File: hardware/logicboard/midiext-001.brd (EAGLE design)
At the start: 72 x 72 mm, 29 parts, among them IC1 74ALS05N, IC2 LTC485N, IC3 LTC485N, J1 PWR, J2 MIDIOUT, J3 MIDIIN, J4 LED, J5 MIDIRX, J6 MIDITX, J7 LED

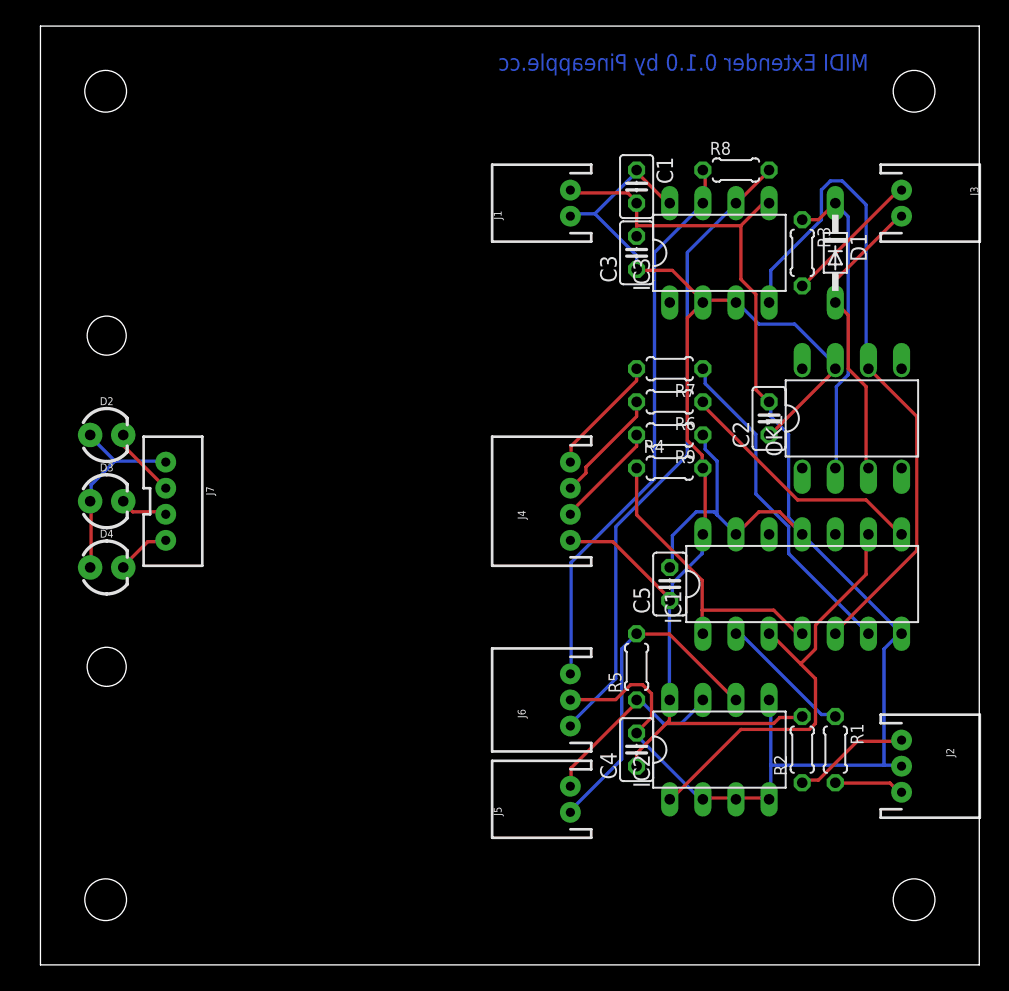
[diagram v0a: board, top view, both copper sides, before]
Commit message: Removed LED panel from main logic board.
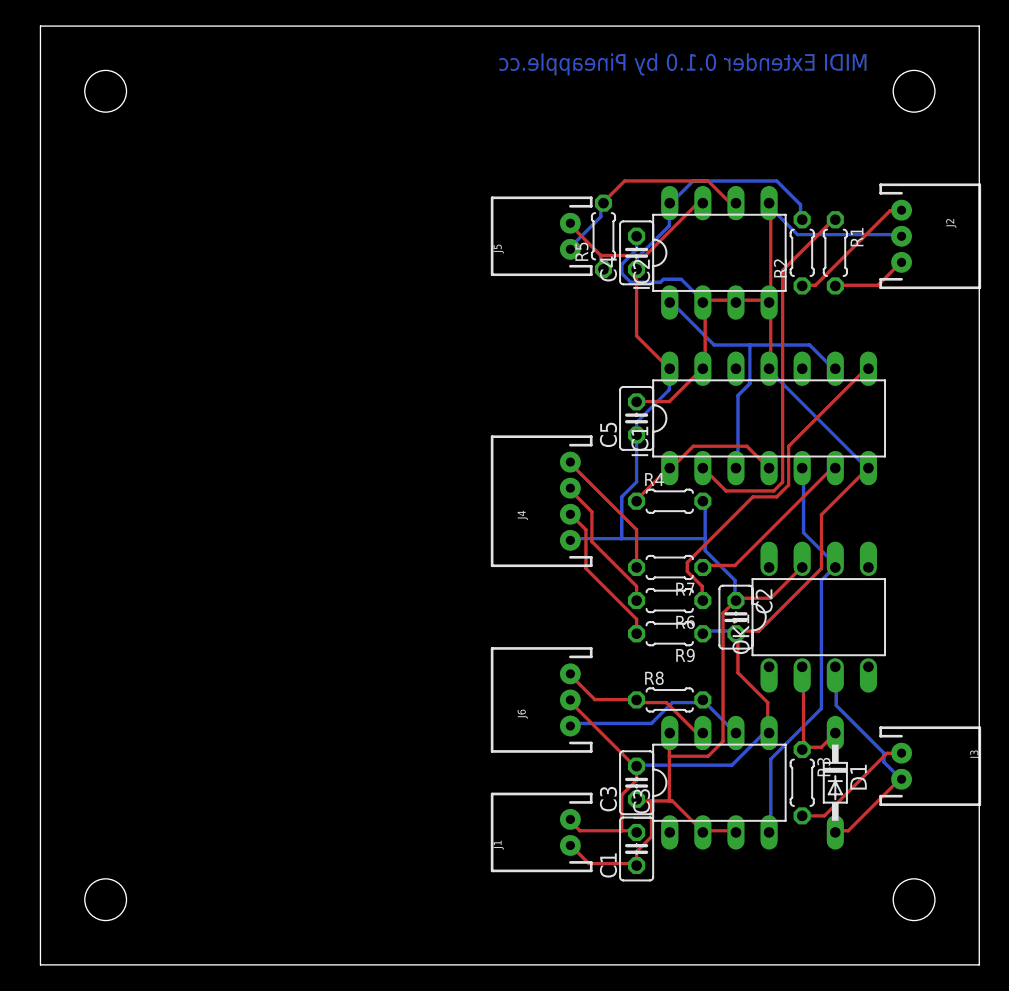
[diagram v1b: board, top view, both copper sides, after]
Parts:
- removed D2: PWR, SparkFun-LED:LED_3MM
- removed D3: OUT, SparkFun-LED:LED_3MM
- removed D4: IN, SparkFun-LED:LED_3MM
- removed J7: LED, SparkFun-Connectors:JST-4-PTH-VERT
- moved C1 50.8 mm to (45.7, 8.89), turned to 90 degrees
- moved J1 48.3 mm to (40.6, 10.2)
- moved J5 43.2 mm to (40.6, 55.9)
- moved J3 43.2 mm to (66.0, 15.2)
- moved R8 41.0 mm to (48.3, 20.3)
- moved C3 40.6 mm to (45.7, 14.0)
- moved D1 40.6 mm to (61.0, 14.0)
- moved IC3 40.6 mm to (52.1, 14.0)
- moved J2 40.6 mm to (66.0, 55.9)
- moved R3 40.6 mm to (58.4, 14.0)
- moved C4 38.1 mm to (45.7, 54.6)
- moved IC2 38.1 mm to (52.1, 54.6)
- moved R1 38.1 mm to (61.0, 54.6)
- moved R2 38.1 mm to (58.4, 54.6)
- moved R5 33.1 mm to (43.2, 55.9)
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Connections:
- removed net N$11: D3.K, J7.3
- removed net N$12: D4.K, J7.4
- removed net N$4: D2.A, D3.A, D4.A, J7.1
- removed net N$5: D2.K, J7.2
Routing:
- net TX+: track 48.9 -> 14.7 mm
- net TX-: track 43.0 -> 12.2 mm
- net COM2: track 52.0 -> 31.2 mm
- net N$2: track 10.4 -> 29.0 mm
- net N$4: track 15.7 -> 0.00 mm
- net N$15: track 24.2 -> 9.38 mm
- net N$6: track 25.7 -> 13.4 mm
- net N$3: track 23.2 -> 12.7 mm
- net N$1: track 34.1 -> 24.7 mm
- net RX+: track 25.5 -> 16.2 mm
- net GND: track 129.2 -> 122.1 mm
- net VCC: track 101.5 -> 108.3 mm
- net N$7: track 19.6 -> 25.2 mm
- net N$5: track 5.42 -> 0.00 mm
- net MIDIRX-: track 22.6 -> 17.6 mm
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
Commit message: Fixed values.
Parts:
- R6, R7, R9: value 220 -> 330
- moved C1 35.7 mm to (10.2, 11.4)
- moved C2 35.7 mm to (17.8, 29.2)
- moved C3 35.7 mm to (10.2, 16.5)
- moved C4 35.7 mm to (10.2, 57.1)
- moved C5 35.7 mm to (10.2, 44.5)
- moved D1 35.7 mm to (25.4, 16.5)
- moved IC1 35.7 mm to (20.3, 44.5)
- moved IC2 35.7 mm to (16.5, 57.1)
- moved IC3 35.7 mm to (16.5, 16.5)
- moved J1 35.7 mm to (5.08, 12.7)
- moved J2 35.7 mm to (30.5, 58.4)
- moved J3 35.7 mm to (30.5, 12.7)
- moved J4 35.7 mm to (5.08, 38.1)
- moved J5 35.7 mm to (5.08, 58.4)
- moved J6 35.7 mm to (5.08, 22.9)
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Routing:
- net MIDIRX-: track 17.6 -> 19.3 mm
- net MIDIRX+: track 9.61 -> 8.20 mm
- net GND: track 122.1 -> 121.4 mm
- net N$7: track 25.2 -> 24.5 mm
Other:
- board size 72 x 72 mm -> 36 x 72 mm
- board text added: "LED"
- board text added: "MIDI Extender 1.0.0 by Pineapple"
- board text added: "MIDIIN"
- board text added: "MIDIOUT"
- board text added: "PWR"
- board text added: "RX"
- board text added: "TX"
- board text removed: "MIDI Extender 0.1.0 by Pineapple.cc"

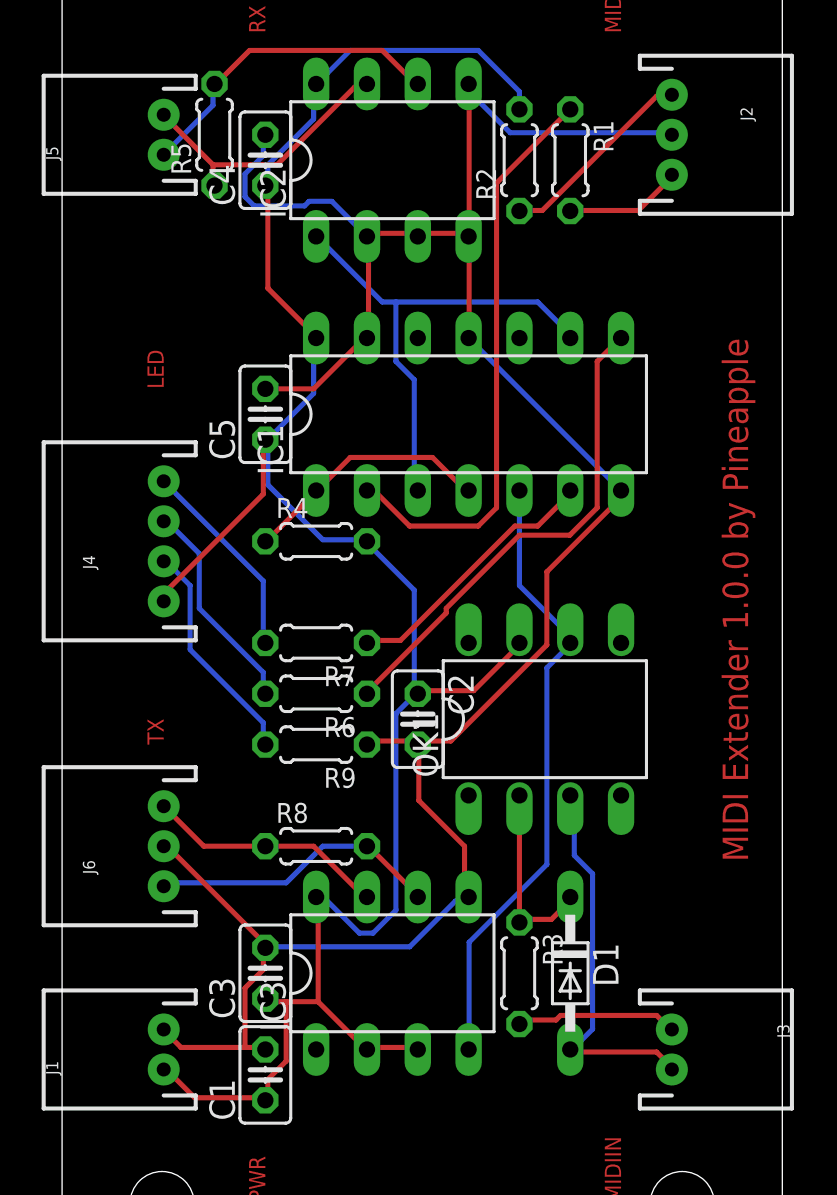
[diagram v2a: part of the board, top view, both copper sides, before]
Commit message: Renumbered components.
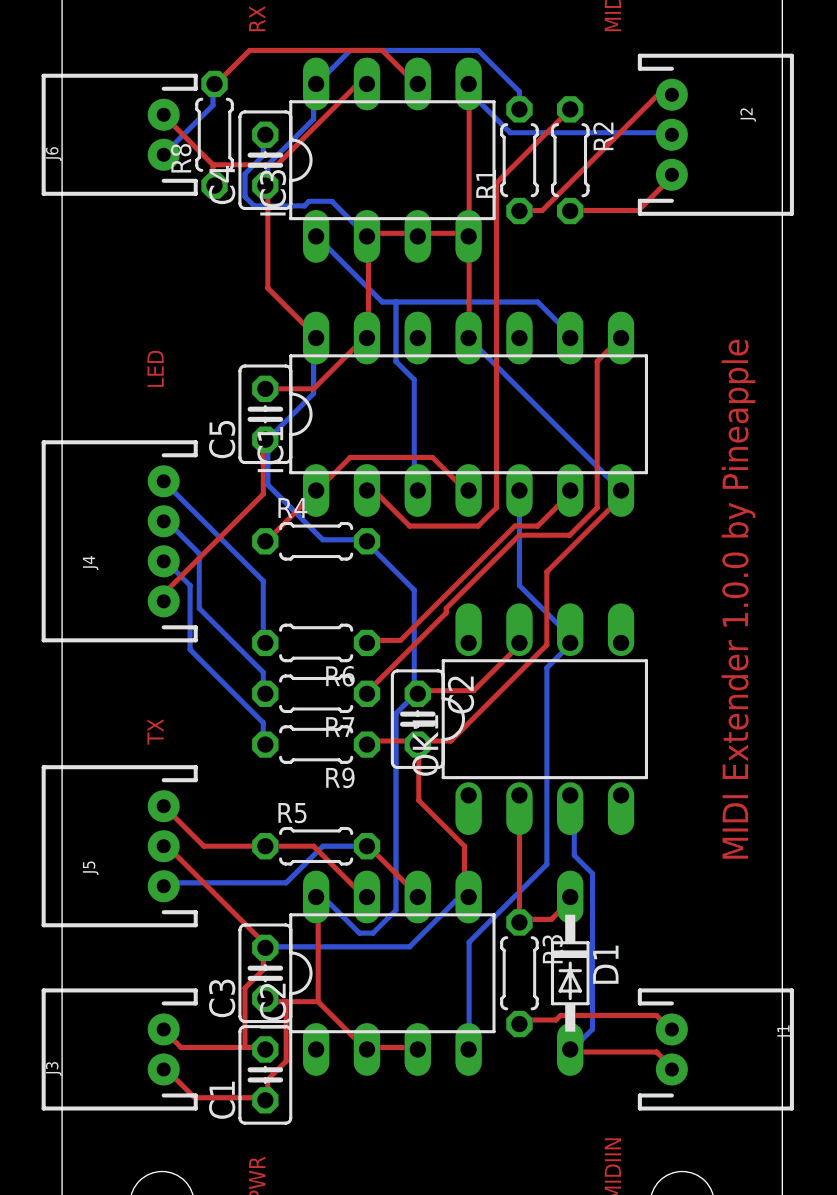
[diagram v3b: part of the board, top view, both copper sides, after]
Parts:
- J1: value PWR -> MIDIIN
- J3: value MIDIIN -> PWR
- J5: value MIDIRX -> MIDITX; device SparkFun-Connectors:JST-2-PTH -> SparkFun-Connectors:JST-3-PTH
- J6: value MIDITX -> MIDIRX; device SparkFun-Connectors:JST-3-PTH -> SparkFun-Connectors:JST-2-PTH
- R4: value 220 -> 10k
- moved IC2 40.6 mm to (16.5, 16.5)
- moved IC3 40.6 mm to (16.5, 57.1)
- moved R5 35.9 mm to (12.7, 22.9), turned to 0 degrees
- moved R8 35.9 mm to (7.62, 58.4), turned to 90 degrees
- moved J5 35.6 mm to (5.08, 22.9)
- moved J6 35.6 mm to (5.08, 58.4)
- moved J1 25.4 mm to (30.5, 12.7), turned to 270 degrees
- moved J3 25.4 mm to (5.08, 12.7), turned to 90 degrees
- moved R6 2.54 mm to (12.7, 33.0)
- moved R7 2.54 mm to (12.7, 30.5)
- moved R1 2.54 mm to (22.9, 57.1), turned to 90 degrees
- moved R2 2.54 mm to (25.4, 57.1), turned to 270 degrees
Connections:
- net COM2: now also IC2.4; no longer IC3.4
- net GND: now also IC3.2, IC3.3, IC3.4, J3.2, J5.2; no longer IC2.2, IC2.3, IC2.4, J1.2, J6.2
- net MIDIRX+: now also J1.1; no longer J3.1
- net MIDIRX-: now also J1.2; no longer J3.2
- net MIDITX+: now also R1.1; no longer R2.1
- net MIDITX-: now also R2.2; no longer R1.2
- net N$1: now also IC3.1; no longer IC2.1
- net N$2: now also R2.1; no longer R1.1
- net N$6: now also R6.1; no longer R7.1
- net N$7: now also R7.1; no longer R6.1
- net N$8: now also R6.2; no longer R7.2
- net N$9: now also R7.2; no longer R6.2
- net RX+: now also IC3.6, J6.1, R8.2; no longer IC2.6, J5.1, R5.2
- net RX-: now also IC3.7, J6.2, R8.1; no longer IC2.7, J5.2, R5.1
- net TX+: now also IC2.6, J5.1, R5.2; no longer IC3.6, J6.1, R8.2
- net TX-: now also IC2.7, J5.3, R5.1; no longer IC3.7, J6.3, R8.1
- net VCC: now also IC2.2, IC2.3, J3.1, R1.2; no longer IC3.2, IC3.3, J1.1, R2.2

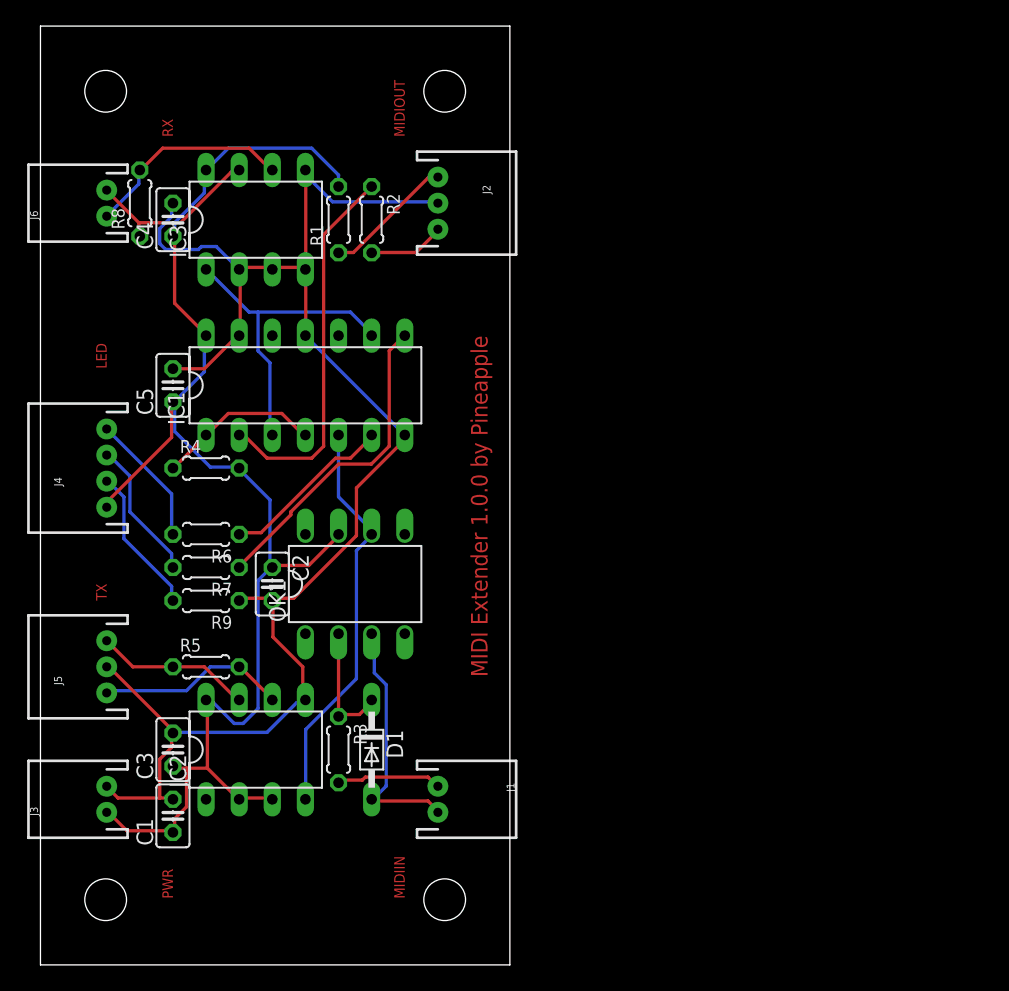
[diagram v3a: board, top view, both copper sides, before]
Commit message: Changed layout.
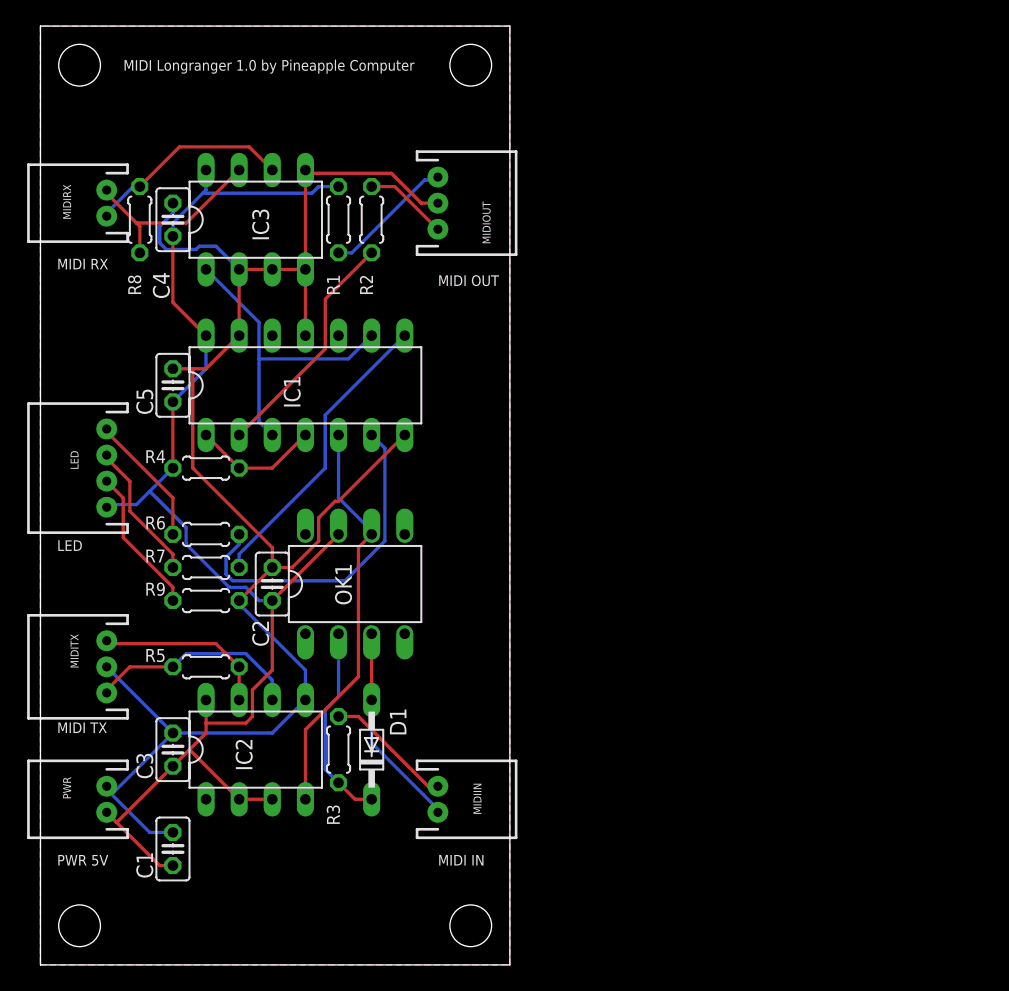
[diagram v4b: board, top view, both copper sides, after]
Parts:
- LED: value LED -> (none)
- MIDIIN: value MIDIIN -> (none)
- MIDIOUT: value MIDIOUT -> (none)
- MIDIRX: value MIDIRX -> (none)
- MIDITX: value MIDITX -> (none)
- PWR: value PWR -> (none)
- moved C1 2.54 mm to (10.2, 8.89)
- moved R8 1.27 mm to (7.62, 57.1)
- turned C2 to 90 degrees
- turned D1 to 90 degrees
- turned R2 to 90 degrees
- turned R3 to 90 degrees
- turned R4 to 180 degrees
- turned R5 to 180 degrees
- renumbered J1 to MIDIIN, J2 to MIDIOUT, J3 to PWR, J4 to LED, J5 to MIDITX, J6 to MIDIRX
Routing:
- net N$6: track 13.4 -> 25.7 mm
- net N$2: track 29.1 -> 18.2 mm
- net GND: track 121.4 -> 129.6 mm
- net N$15: track 9.45 -> 15.3 mm
- net VCC: track 108.8 -> 104.1 mm
- net MIDIRX-: track 19.3 -> 15.8 mm
- net N$3: track 12.6 -> 9.72 mm
- net TX+: track 14.7 -> 16.4 mm
- net MIDIRX+: track 8.20 -> 9.85 mm
- net TX-: track 12.0 -> 13.7 mm
- net RX-: track 13.9 -> 15.4 mm
- net N$7: track 24.5 -> 23.0 mm
- net N$1: track 24.8 -> 24.2 mm
- net MIDITX-: track 5.87 -> 6.48 mm
- added copper zone on layer 1, net GND
- added copper zone on layer 16, net GND
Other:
- board text added: "MIDI IN"
- board text added: "MIDI Longranger 1.0 by Pineapple Computer"
- board text added: "MIDI OUT"
- board text added: "MIDI RX"
- board text added: "MIDI TX"
- board text added: "PWR 5V"
- board text removed: "MIDI Extender 1.0.0 by Pineapple"
- board text removed: "MIDIIN"
- board text removed: "MIDIOUT"
- board text removed: "PWR"
- board text removed: "RX"
- board text removed: "TX"

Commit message: Changed silk pattern.
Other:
- board text added: "MIDI Longranger 1.0.0 by Pineapple Computer"
- board text removed: "MIDI Longranger 1.0 by Pineapple Computer"
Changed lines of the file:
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@@
 <hole x="33" y="69" drill="3.2"/>
 <hole x="3" y="69" drill="3.2"/>
-<text x="6.35" y="68.58" size="0.8128" layer="25">MIDI Longranger 1.0 by Pineapple Computer</text>
+<text x="6.35" y="68.58" size="0.8128" layer="25">MIDI Longranger 1.0.0 by Pineapple Computer</text>
 <text x="30.48" y="52.07" size="0.8128" layer="25">MIDI OUT</text>
 <text x="30.48" y="7.62" size="0.8128" layer="25">MIDI IN</text>
